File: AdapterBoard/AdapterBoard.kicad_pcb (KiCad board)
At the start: 2 copper layers, 100 x 100 mm, 80 parts, among them J1 Conn_01x06, J10 Conn_01x01, J11 Conn_01x02, J12 Conn_01x01, J13 Conn_01x02, J14 Conn_01x01, J15 Conn_01x02, J16 Conn_01x01, J17 Conn_01x02, J18 Conn_01x01, J19 Conn_01x02, J2 Conn_01x06, J20 Conn_01x01, J21 Conn_01x02, J22 Conn_01x01, J23 Conn_01x02, J24 Conn_01x01, J25 Conn_01x01, J26 Conn_01x06, J27 Conn_01x01, J28 Conn_01x04, J29 Conn_01x06, J3 Conn_01x06, J30 Conn_01x06, J31 Conn_01x04, J32 Conn_01x01, J33 Conn_01x06, J34 Conn_01x01, J35 Conn_01x01, J36 Conn_01x01, J37 Conn_01x01, J38 Conn_01x06, J39 Conn_01x01, J4 Conn_01x06, J40 Conn_01x04, J41 Conn_01x06, J42 Conn_01x06, J43 Conn_01x04, J44 Conn_01x01, J45 Conn_01x06, J46 Conn_01x01, J47 Conn_01x01, J48 Conn_01x06, J49 Conn_01x04, J5 Conn_01x06, J50 Conn_01x01, J51 Conn_01x06, J52 Conn_01x01, J53 Conn_01x01, J54 Conn_01x06, J55 Conn_01x04, J56 Conn_01x01, J57 Conn_01x06, J58 Conn_01x01, J59 Conn_01x04, J6 Conn_01x06, J60 Conn_02x13_Odd_Even, J61 Conn_01x04, J62 Conn_01x04, J63 Conn_01x13, J64 Conn_01x13, J7 Conn_01x06, J8 Conn_01x06, J9 Conn_01x02

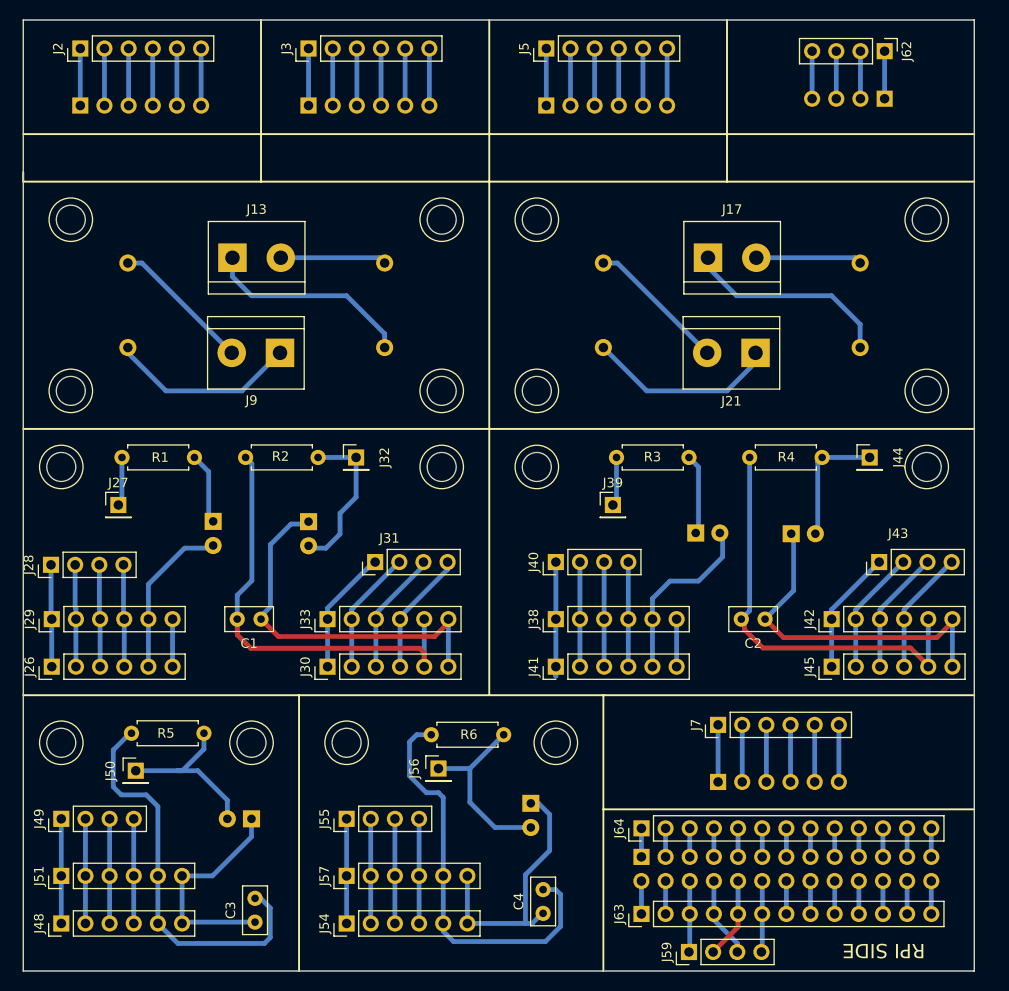
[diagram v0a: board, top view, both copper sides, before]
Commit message: Added CAD models
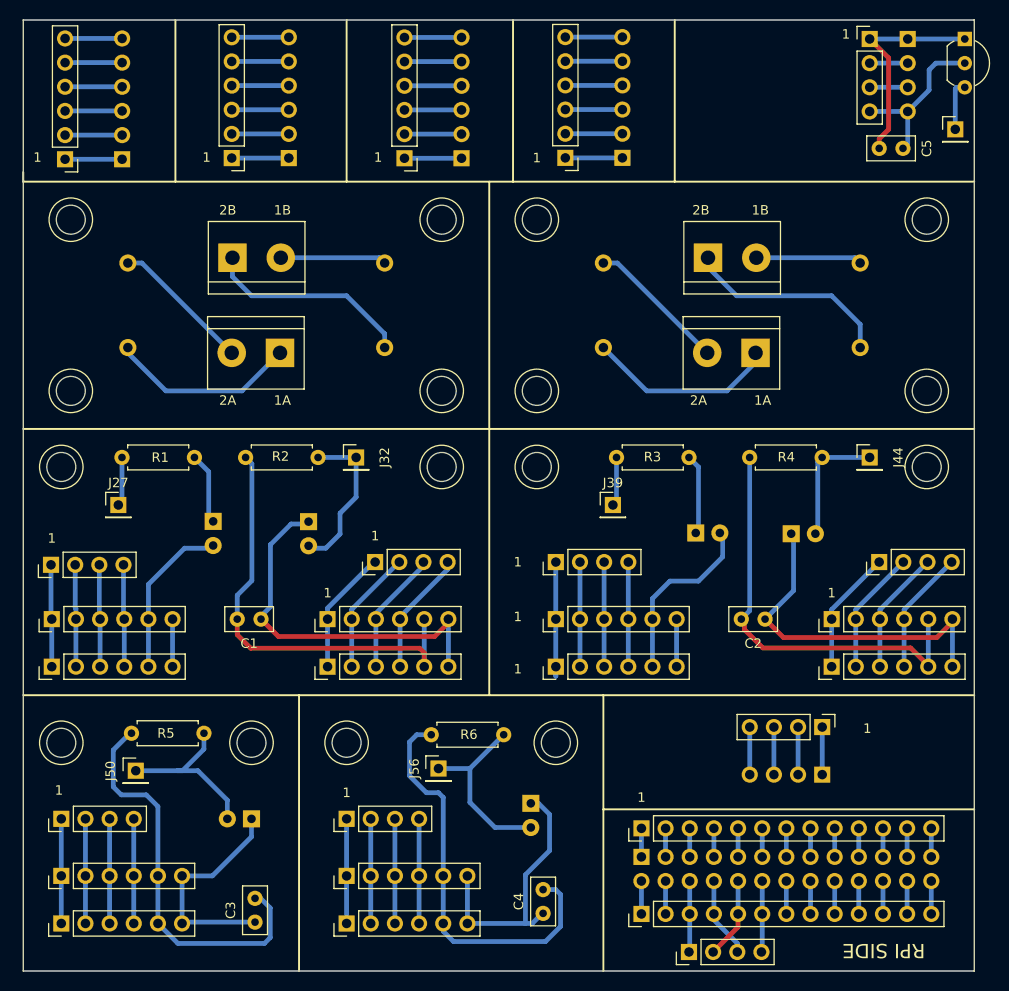
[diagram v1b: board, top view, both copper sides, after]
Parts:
- added C5: 100 nF, Capacitors_THT:C_Disc_D5.0mm_W2.5mm_P2.50mm, F.Cu at (120.0, 43.5)
- added J65: Conn_01x01, Pin_Headers:Pin_Header_Straight_1x01_Pitch2.54mm, F.Cu at (128.0, 41.5)
- added J66: Conn_01x03, TO_SOT_Packages_THT:TO-92_Inline_Wide, F.Cu at (129.0, 32.0)
- added J67: Conn_01x06, Pin_Headers:Pin_Header_Straight_1x06_Pitch2.54mm, F.Cu at (87.0, 44.5)
- added J68: Conn_01x06, Pin_Headers:Pin_Header_Straight_1x06_Pitch2.54mm, B.Cu at (93.0, 44.5)
- J7, J8: value Conn_01x06 -> Conn_01x04; footprint Pin_Headers:Pin_Header_Straight_1x06_Pitch2.54mm -> Pin_Headers:Pin_Header_Straight_1x04_Pitch2.54mm
- moved J8 80.6 mm to (123.0, 32.0), turned to 180 degrees
- moved J7 73.9 mm to (119.0, 32.0), turned to 0 degrees
- moved J61 71.4 mm to (114.0, 109.3)
- moved J62 71.4 mm to (114.0, 104.3)
- moved J5 18.9 mm to (70.1, 44.5), turned to 180 degrees
- moved J3 14.1 mm to (51.9, 44.5), turned to 180 degrees
- moved J2 11.8 mm to (34.4, 44.6), turned to 180 degrees
- moved J6 10.5 mm to (76.1, 44.5), turned to 0 degrees
- moved J1 7.16 mm to (40.4, 44.6), turned to 0 degrees
- moved J4 5.90 mm to (57.9, 44.5), turned to 0 degrees
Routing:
- net Net-(C5-Pad1): track 6.00 -> 22.7 mm
- net Net-(C5-Pad2): track 6.00 -> 17.8 mm
- net Net-(J7-Pad6): track 6.00 -> 0.00 mm
- net Net-(J7-Pad5): track 6.00 -> 0.00 mm
- net Net-(J67-Pad6): track 0.00 -> 6.00 mm
- net Net-(J67-Pad5): track 0.00 -> 6.00 mm
- net Net-(J67-Pad4): track 0.00 -> 6.00 mm
- net Net-(J67-Pad3): track 0.00 -> 6.00 mm
- net Net-(J67-Pad2): track 0.00 -> 6.00 mm
- net Net-(J67-Pad1): track 0.00 -> 6.00 mm
- net Net-(J65-Pad1): track 0.00 -> 5.32 mm
- net Net-(J7-Pad3): track 6.00 -> 4.00 mm
- net Net-(J7-Pad2): track 6.00 -> 4.00 mm
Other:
- board text added: "1"
- board text added: "1A"
- board text added: "1B"
- board text added: "2A"
- board text added: "2B"

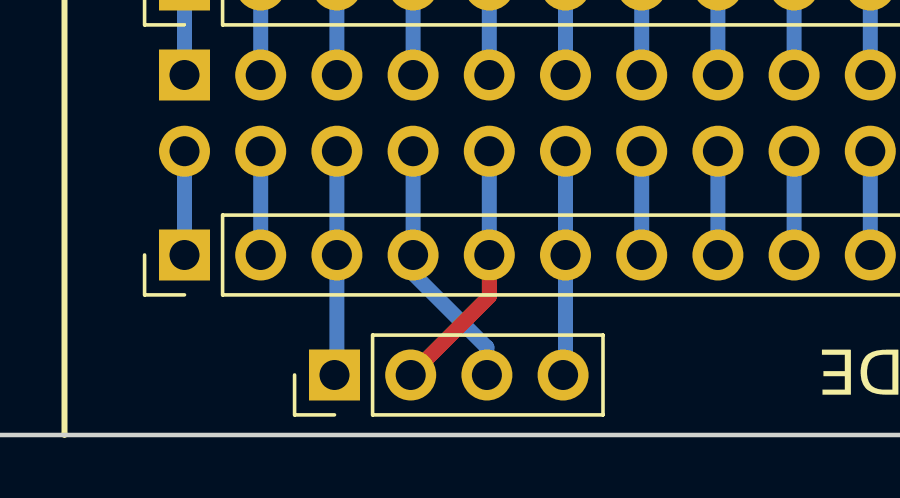
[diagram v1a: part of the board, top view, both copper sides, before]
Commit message: Added second microphone to keypad
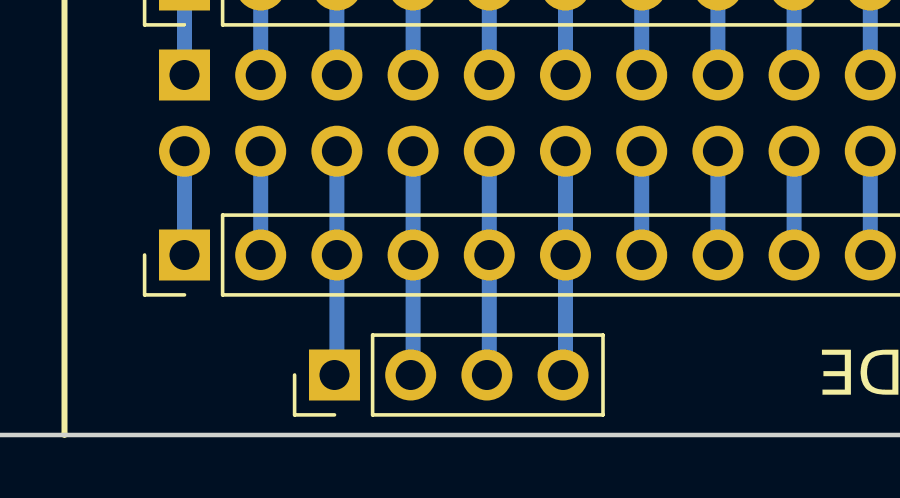
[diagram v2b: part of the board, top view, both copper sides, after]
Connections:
- J60 pad 10: Net-(J59-Pad2) -> Net-(J59-Pad3)
- J60 pad 8: Net-(J59-Pad3) -> Net-(J59-Pad2)
- J63 pad 4: Net-(J59-Pad3) -> Net-(J59-Pad2)
- J63 pad 5: Net-(J59-Pad2) -> Net-(J59-Pad3)
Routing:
- net Net-(J59-Pad3): track 8.48 -> 7.49 mm
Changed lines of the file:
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@@
     (links 165)
     (no_connects 0)
-    (area 29.252381 28.495 133.635 132.747619)
+    (area 29.924999 29.924999 130.075001 130.075001)
     (thickness 1.6)
     (drawings 70)
@@
       (net 82 "Net-(J60-Pad7)"))
     (pad 8 thru_hole oval (at 2.54 -7.62 270) (size 1.7 1.7) (drill 1) (layers *.Cu *.Mask)
-      (net 75 "Net-(J59-Pad3)"))
+      (net 74 "Net-(J59-Pad2)"))
     (pad 9 thru_hole oval (at 0 -10.16 270) (size 1.7 1.7) (drill 1) (layers *.Cu *.Mask)
       (net 83 "Net-(J60-Pad9)"))
     (pad 10 thru_hole oval (at 2.54 -10.16 270) (size 1.7 1.7) (drill 1) (layers *.Cu *.Mask)
-      (net 74 "Net-(J59-Pad2)"))
+      (net 75 "Net-(J59-Pad3)"))
     (pad 11 thru_hole oval (at 0 -12.7 270) (size 1.7 1.7) (drill 1) (layers *.Cu *.Mask)
       (net 84 "Net-(J60-Pad11)"))
@@
       (net 73 "Net-(J59-Pad1)"))
     (pad 4 thru_hole oval (at 0 7.62 90) (size 1.7 1.7) (drill 1) (layers *.Cu *.Mask)
-      (net 75 "Net-(J59-Pad3)"))
-    (pad 5 thru_hole oval (at 0 10.16 90) (size 1.7 1.7) (drill 1) (layers *.Cu *.Mask)
       (net 74 "Net-(J59-Pad2)"))
+    (pad 5 thru_hole oval (at 0 10.16 90) (size 1.7 1.7) (drill 1) (layers *.Cu *.Mask)
+      (net 75 "Net-(J59-Pad3)"))
     (pad 6 thru_hole oval (at 0 12.7 90) (size 1.7 1.7) (drill 1) (layers *.Cu *.Mask)
       (net 76 "Net-(J59-Pad4)"))
@@
   (segment (start 100.08 127.92) (end 100 128) (width 0.5) (layer B.Cu) (net 73))
   (segment (start 100.08 120.54) (end 100.08 124) (width 0.5) (layer B.Cu) (net 73))
-  (segment (start 105.16 124) (end 105.16 125.38) (width 0.5) (layer F.Cu) (net 74))
-  (segment (start 105.16 125.38) (end 102.54 128) (width 0.5) (layer F.Cu) (net 74))
-  (segment (start 105.16 120.54) (end 105.16 124) (width 0.5) (layer B.Cu) (net 74))
-  (segment (start 102.62 124) (end 102.62 124.62) (width 0.5) (layer B.Cu) (net 75))
-  (segment (start 102.62 124.62) (end 105.08 127.08) (width 0.5) (layer B.Cu) (net 75))
-  (segment (start 105.08 127.08) (end 105.08 128) (width 0.5) (layer B.Cu) (net 75))
-  (segment (start 102.62 120.54) (end 102.62 124) (width 0.5) (layer B.Cu) (net 75))
+  (segment (start 102.62 124) (end 102.62 127.92) (width 0.5) (layer B.Cu) (net 74) (status C00000))
+  (segment (start 102.62 127.92) (end 102.54 128) (width 0.5) (layer B.Cu) (net 74) (status C00000))
+  (segment (start 102.62 124) (end 102.62 124.62) (width 0.5) (layer B.Cu) (net 74))
+  (segment (start 102.62 120.54) (end 102.62 124) (width 0.5) (layer B.Cu) (net 74))
+  (segment (start 105.16 124) (end 105.16 127.92) (width 0.5) (layer B.Cu) (net 75) (status C00000))
+  (segment (start 105.16 127.92) (end 105.08 128) (width 0.5) (layer B.Cu) (net 75) (status C00000))
+  (segment (start 105.16 120.54) (end 105.16 124) (width 0.5) (layer B.Cu) (net 75))
   (segment (start 107.7 124) (end 107.7 127.92) (width 0.5) (layer B.Cu) (net 76))
   (segment (start 107.7 127.92) (end 107.62 128) (width 0.5) (layer B.Cu) (net 76))

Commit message: new commit
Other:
- net class Default removed
